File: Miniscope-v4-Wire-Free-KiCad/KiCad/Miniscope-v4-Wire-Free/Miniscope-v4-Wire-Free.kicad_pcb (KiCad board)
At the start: 6 copper layers, 27.6 x 12.2 mm, 114 parts, among them J1 0475710001, J10 Conn_01x01, J11 Conn_01x01, J12 Conn_01x01, J14 Conn_01x01, J15 Conn_01x01, J16 Conn_01x01, J17 Conn_01x01, J18 Conn_01x01, J19 Conn_01x01, J2 Conn_01x04, J20 Conn_01x01, J21 Conn_01x01, J22 Conn_01x01, J23 Conn_01x01, J24 Conn_01x01, J25 Conn_01x01, J26 Conn_01x01, J27 Conn_01x01, J3 Conn_01x04, J4 Conn_01x01, J5 Conn_01x01, J6 Conn_01x01, J7 Conn_01x01, J8 Conn_01x01, J9 Conn_01x01, Q1 NTK3134NT1G, Q2 MMBT3904LP-7B, SW1 TL3780AF330QG, U1 LTC3554, U2 HV892, U3 LTC3218, U4 MAX13030EETE+BGA, U5 TSOP57438TT1, U6 ATSAMD51J20A-UUT-EFP, U7 NCP163AMX330TBG, U8 NOIP1SN0480A, U9 LMV321IDCKR, Y2 Crystal

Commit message: Update public repository
- Made copy to a public repository
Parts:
- added ?: , , F.Cu at (103.6, 61.0)
- added R22: 10K, Resistor_SMD:R_0201_0603Metric, F.Cu at (85.0, 65.0)
- added REF**: MountingHole_2.1mm, MountingHole:MountingHole_2.1mm, F.Cu at (103.6, 67.9)
- D1: value LXZ1-PR01 -> LXZ1-PB01
- moved C42 0.42 mm to (85.0, 63.8)
- moved C43 0.37 mm to (85.2, 65.9), turned to 0 degrees
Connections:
- U1 pad 19: Net-(U1-Pad19) -> unconnected-(U1-SUSP-Pad19)
- U1 pad 4: Net-(U1-Pad4) -> unconnected-(U1-PGOOD-Pad4)
- U2 pad 9: Net-(U2-Pad9) -> unconnected-(U2-NC-Pad9)
- U6 pad B3: Net-(U6-PadB3) -> unconnected-(U6A-PA27-PadB3)
- U6 pad B6: Net-(U6-PadB6) -> unconnected-(U6A-PB31-PadB6)
- U6 pad C6: Net-(U6-PadC6) -> unconnected-(U6A-PB03-PadC6)
- U6 pad D6: Net-(U6-PadD6) -> unconnected-(U6A-PA03-PadD6)
- U6 pad D7: Net-(U6-PadD7) -> unconnected-(U6A-PB04-PadD7)
- U6 pad E6: Net-(U6-PadE6) -> unconnected-(U6A-PB07-PadE6)
- U6 pad E7: Net-(U6-PadE7) -> unconnected-(U6A-PB06-PadE7)
- U6 pad F5: Net-(U6-PadF5) -> unconnected-(U6A-PB08-PadF5)
- U8 pad B11: Net-(U8-PadB11) -> unconnected-(U8-CLK_OUTP-PadB11)
- U8 pad B9: Net-(U8-PadB9) -> unconnected-(U8-DOUT0-PadB9)
- U8 pad C10: Net-(U8-PadC10) -> unconnected-(U8-CLK_OUTN-PadC10)
- U8 pad C11: Net-(U8-PadC11) -> unconnected-(U8-DOUTP-PadC11)
- U8 pad C9: Net-(U8-PadC9) -> unconnected-(U8-DOUT1-PadC9)
- U8 pad D10: Net-(U8-PadD10) -> unconnected-(U8-DOUTN-PadD10)
- U8 pad D11: Net-(U8-PadD11) -> unconnected-(U8-SYNCP-PadD11)
- U8 pad E10: Net-(U8-PadE10) -> unconnected-(U8-SYNCN-PadE10)
- U8 pad E11: Net-(U8-PadE11) -> unconnected-(U8-LVDS_CLK_INP-PadE11)
- U8 pad F1: Net-(U8-PadF1) -> unconnected-(U8-CP_RESPD-PadF1)
- U8 pad F10: Net-(U8-PadF10) -> unconnected-(U8-LVDS_CLK_INN-PadF10)
- U8 pad G1: Net-(U8-PadG1) -> unconnected-(U8-CP_CALIB-PadG1)
- U8 pad H1: Net-(U8-PadH1) -> unconnected-(U8-MBSINOUT1-PadH1)
- U8 pad H2: Net-(U8-PadH2) -> unconnected-(U8-MBSINOUT1-PadH2)
- U8 pad H3: Net-(U8-PadH3) -> unconnected-(U8-MBSINOUT2-PadH3)
- U8 pad H4: Net-(U8-PadH4) -> unconnected-(U8-CP_SEL_SAMPLE-PadH4)
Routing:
- net GND: track 80.9 -> 82.4 mm, vias 46 -> 45
- net /nRESET: track 8.70 -> 9.79 mm
- net +1V8: track 62.4 -> 63.0 mm
- net /SPI1_NSS: vias 4 -> 3
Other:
- rule pad_to_mask_clearance: 0.0254 -> 0
- board text added: "C10"
- board text added: "C11"
- board text added: "C12"
- board text added: "C13"
- board text added: "C14"
- board text added: "C15"
- board text added: "C17"
- board text added: "C18"
- board text added: "C19"
- board text added: "C20"
- board text added: "C22"
- board text added: "C23"
- board text added: "C24"
- board text added: "C25"
- board text added: "C27"
- board text added: "C28"
- board text added: "C29"
- board text added: "C3"
- board text added: "C30"
- board text added: "C36"
- board text added: "C37"
- board text added: "C38"
- board text added: "C4"
- board text added: "C40"
- board text added: "C41"
- board text added: "C42"
- board text added: "C43"
- board text added: "C44"
- board text added: "C45"
- board text added: "C46"
- board text added: "C47"
- board text added: "C48"
- board text added: "C49"
- board text added: "C5"
- board text added: "C53"
- board text added: "C9"
- board text added: "R1"
- board text added: "R16"
- board text added: "R17"
- board text added: "R19"
- board text added: "R21"
- board text added: "V4WF v0.2"
- board text removed: "V4WF v0.1"

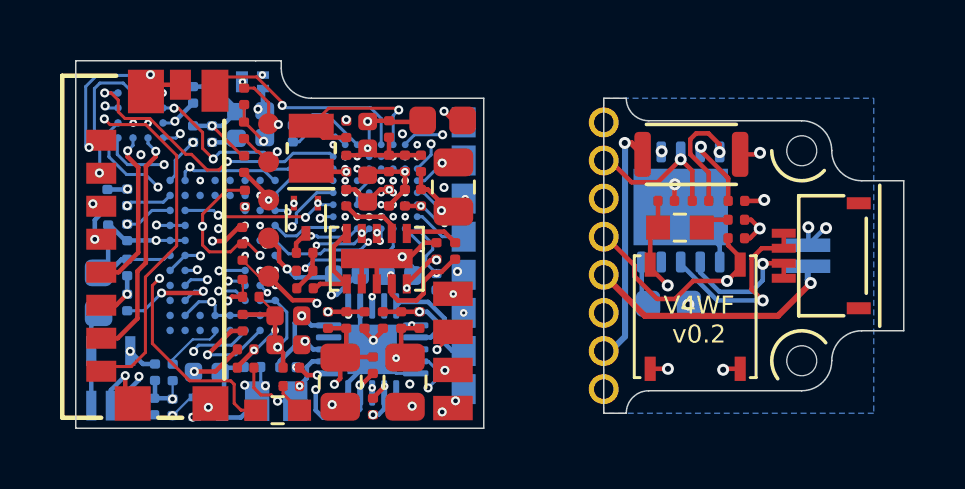
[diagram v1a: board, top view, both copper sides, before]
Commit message: Fix to the PCB project
- Reverted the project to KiCAD 6 to avoid breaking microvias when moving to KiCAD 7 or 8
- SPI_CS now connected again

To do:

- Remove the asterisk on the microcontroller silk layer
- Add gerbers for the new PCB
- Discuss with Daniel which numbering version to use
- Add back the 3D models
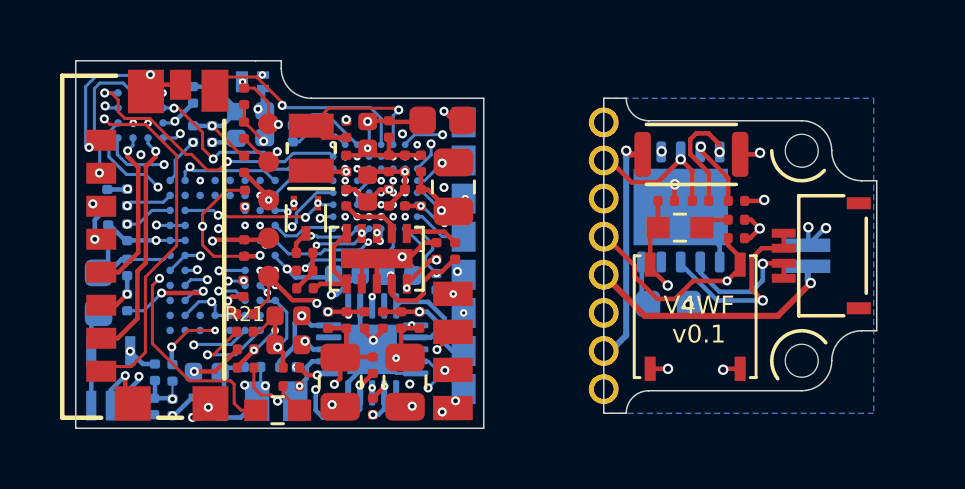
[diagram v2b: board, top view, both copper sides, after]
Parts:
- removed ?: , 
- removed REF**: MountingHole_2.1mm, MountingHole:MountingHole_2.1mm
- added Mount: Conn_1x1_700_Circular_Pad, .Connector:Conn_1x1_700_Circular_Pad, F.Cu at (103.6, 68.0)
- added Mount: Conn_1x1_700_Circular_Pad, .Connector:Conn_1x1_700_Circular_Pad, F.Cu at (103.6, 61.0)
- D1: value LXZ1-PB01 -> LXZ1-PR01
- L3: value BLM18PG471SN1D -> L_Small
- R2: value R_Small_US -> 1K8
- R21: value 47k5 -> 10K; footprint .Resistor:R_0201_0603Metric_ERJ_L -> Custom:R_0201_0603Metric_ERJ_L; moved to F.Cu
- R22: value 10K -> 47k5; footprint Resistor_SMD:R_0201_0603Metric -> Custom:R_0201_0603Metric_ERJ_L; moved to B.Cu
- moved R22 4.15 mm to (82.6, 68.4), turned to -90 degrees
- moved R21 3.09 mm to (85.0, 66.4), turned to 0 degrees
- moved C42 0.42 mm to (85.0, 64.2)
- moved C43 0.37 mm to (85.0, 65.6), turned to 90 degrees
- moved C47 0.31 mm to (85.0, 67.0), turned to 0 degrees
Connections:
- R21 pad 1: Net-(U8-IBIAS_MASTER) -> +1V8
- R21 pad 2: GND -> /nRESET
- R22 pad 1: +1V8 -> Net-(U8-PadE1)
- R22 pad 2: /nRESET -> GND
- U8 pad E1: Net-(U8-IBIAS_MASTER) -> Net-(U8-PadE1)
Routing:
- net Net-(U8-PadE1): track 0.00 -> 2.27 mm, vias 0 -> 2
- net Net-(U8-IBIAS_MASTER): track 2.05 -> 0.00 mm
- net GND: track 82.4 -> 80.8 mm, vias 45 -> 46
- net /SPI1_NSS: vias 3 -> 4
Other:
- board size 27.6 x 12.2 mm -> 26.7 x 12.2 mm
- rule pad_to_mask_clearance: 0 -> 0.0254
- board text added: "V4WF v0.1"
- board text removed: "C10"
- board text removed: "C11"
- board text removed: "C12"
- board text removed: "C13"
- board text removed: "C14"
- board text removed: "C15"
- board text removed: "C17"
- board text removed: "C18"
- board text removed: "C19"
- board text removed: "C20"
- board text removed: "C22"
- board text removed: "C23"
- board text removed: "C24"
- board text removed: "C25"
- board text removed: "C27"
- board text removed: "C28"
- board text removed: "C29"
- board text removed: "C3"
- board text removed: "C30"
- board text removed: "C36"
- board text removed: "C37"
- board text removed: "C38"
- board text removed: "C4"
- board text removed: "C40"
- board text removed: "C41"
- board text removed: "C42"
- board text removed: "C43"
- board text removed: "C44"
- board text removed: "C45"
- board text removed: "C46"
- board text removed: "C47"
- board text removed: "C48"
- board text removed: "C49"
- board text removed: "C5"
- board text removed: "C53"
- board text removed: "C9"
- board text removed: "R1"
- board text removed: "R16"
- board text removed: "R17"
- board text removed: "R19"
- board text removed: "R21"
- board text removed: "V4WF v0.2"

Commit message: Update version number on the PCB
- Updated the version number of the PCB to v1.0
- Removed the asterisk on the microcontroller footprint.
- Removed the resistor number on the newly added resistors (reset and ibias)
- Cleaned up the firmware a bit

To do:

- Do a final check of the PCB and the firmware to ensure that everything is working smoothly
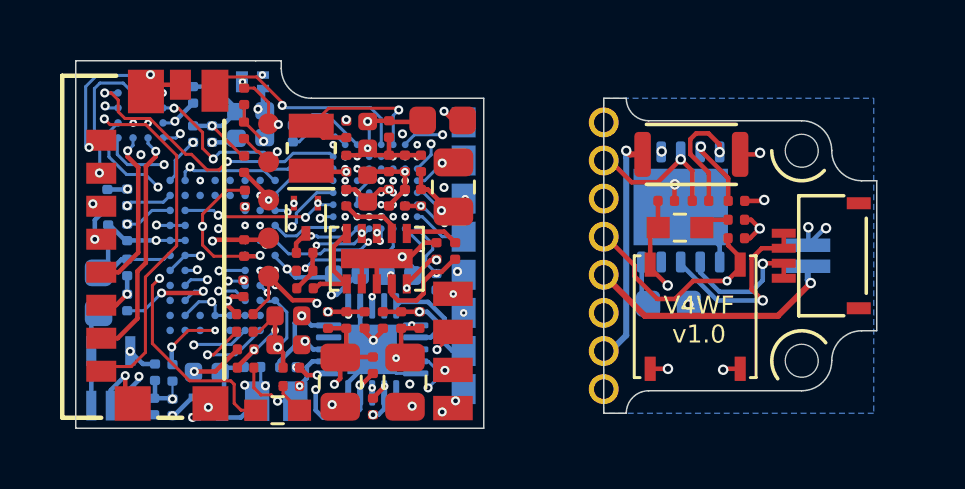
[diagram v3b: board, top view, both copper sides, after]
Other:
- board text added: "V4WF v1.0"
- board text removed: "V4WF v0.1"
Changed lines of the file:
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@@
     (property "Sheetname" "")
     (attr smd)
-    (fp_text reference "R21" (at 0 0) (layer "F.Fab")
+    (fp_text reference "R21" (at 0 0) (layer "F.Fab") hide
       (effects (font (size 1 1) (thickness 0.1)))
     )
@@
       (effects (font (size 1.2 1.2) (thickness 0.12)))
     )
-    (fp_text user "${REFERENCE}" (at 0 0) (layer "F.SilkS")
+    (fp_text user "${REFERENCE}" (at 0 0) (layer "F.SilkS") hide
       (effects (font (size 0.5 0.5) (thickness 0.05)))
     )
@@
       (effects (font (size 1 1) (thickness 0.15)) (justify mirror))
     )
-    (fp_text user "*" (at 0 0 90) (layer "B.SilkS")
+    (fp_text user "*" (at 0 0 90) (layer "B.SilkS") hide
       (effects (font (size 1 1) (thickness 0.15)) (justify mirror))
     )
@@
       (effects (font (size 1.2 1.2) (thickness 0.12)) (justify mirror))
     )
-    (fp_text user "${REFERENCE}" (at 0 0 90) (layer "B.SilkS")
+    (fp_text user "${REFERENCE}" (at 0 0 90) (layer "B.SilkS") hide
       (effects (font (size 0.5 0.5) (thickness 0.05)) (justify mirror))
     )
@@
   (gr_line (start 103.6 60) (end 98.5 60) (layer "Edge.Cuts") (width 0.05))
   (gr_line (start 106.1 62) (end 106.1 67) (layer "Edge.Cuts") (width 0.05))
-  (gr_text "V4WF \nv0.1" (at 99.0198 67.8116) (layer "B.SilkS")
+  (gr_text "V4WF \nv1.0" (at 99.0198 67.8116) (layer "B.SilkS")
     (effects (font (size 0.6 0.6) (thickness 0.08)) (justify mirror))
   )
-  (gr_text "V4WF \nv0.1" (at 100.175 66.6336) (layer "F.SilkS")
+  (gr_text "V4WF \nv1.0" (at 100.175 66.6336) (layer "F.SilkS")
     (effects (font (size 0.6 0.6) (thickness 0.08)))
   )

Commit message: Added part numbers to all the components.
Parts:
- D2, D3: value LED_Small_ALT -> LTST-C191KEKT
- J10, J11, J12, J14, J15, J16, J17, J18, J19, J20, J21, J22, J23, J24, J25, J26, J27, J4, J5, J6, J7, J8, J9: value Conn_01x01 -> DNP
- J2: value Conn_01x04 -> DNP
- L3: value L_Small -> BLM18PG471SN1D
- R1, R17: value 25K -> 24.9k
- R12: value DNL -> DNP
- R13: value 400K -> 402k
- R15: value 37K -> 37.4k
- R18: value R_Small_US -> 1k8
- R3: value 1.25M -> 1.27M
- R6: value 649K -> 649k
- R7, R8: value 2.2K -> 2.2k
- R9: value 8.2K -> 8.2k
- U4: value MAX13030EETE+BGA -> MAX13030EEBE+T
- U6: value ATSAMD51J20A-UUT-EFP -> ATSAMD51J20A
- U8: value NOIP1SN0480A -> NOIP1SN0480A-STI
- Y2: value Crystal -> XTAL 32.7680KHZ
